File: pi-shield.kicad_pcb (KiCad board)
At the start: 4 copper layers, 65 x 56 mm, 52 parts, among them J1 Conn_02x20_Odd_Even, J10 Conn_01x04, J11 0530470210, J12 Conn_01x03, J2 Conn_01x04, J3 Conn_01x04, J4 0530470210, J5 Conn_01x05, J6 Conn_01x07, J7 0530471410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

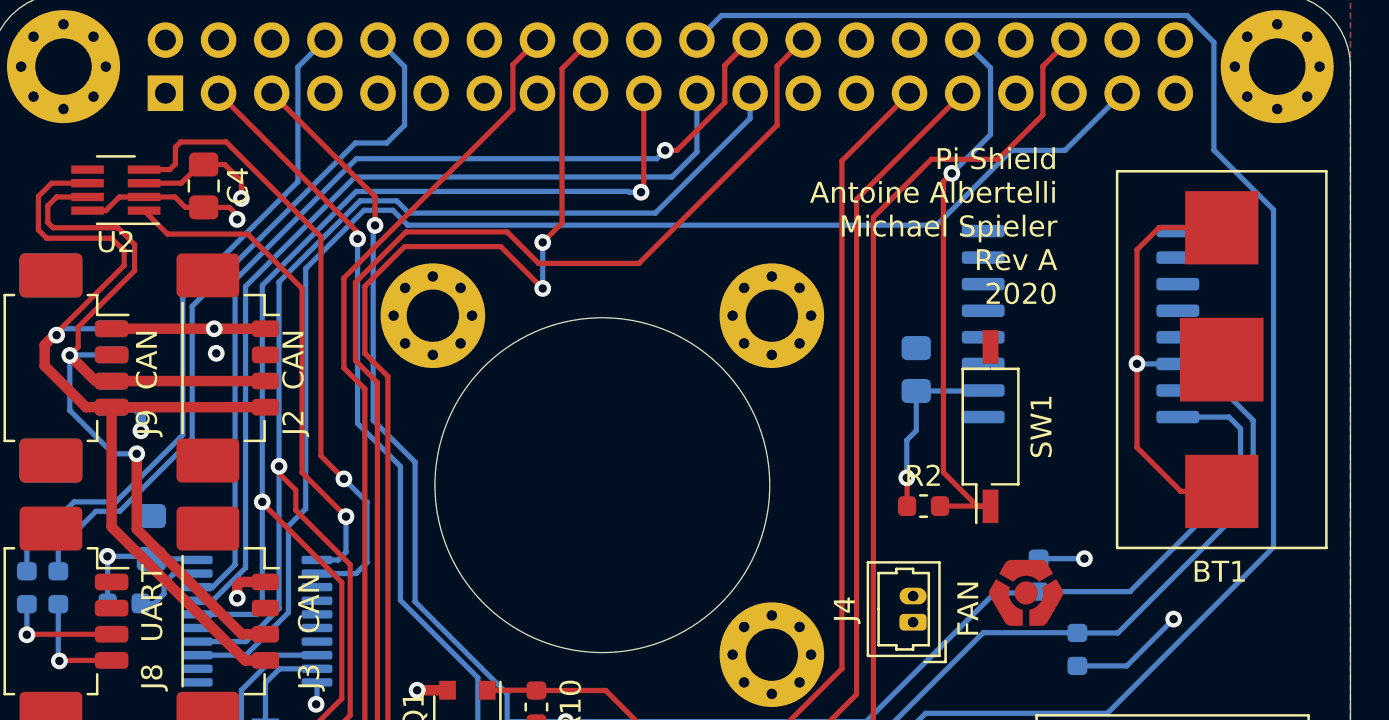
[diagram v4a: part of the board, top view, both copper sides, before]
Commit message: Add missing 3d object
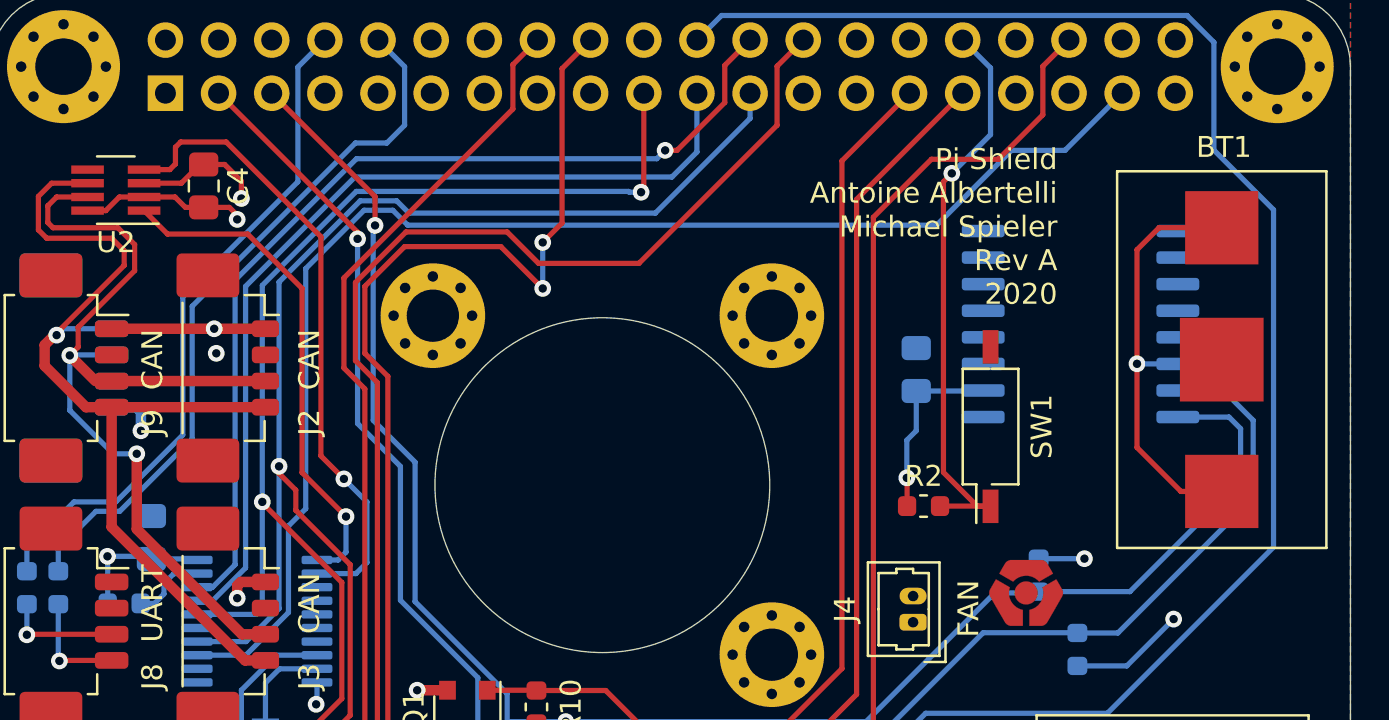
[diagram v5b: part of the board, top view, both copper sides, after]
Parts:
- turned BT1 to 270 degrees

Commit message: Corrections taking into account @nuft remarks
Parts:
- moved R10 4.53 mm to (66.8, 72.3)
- moved Q1 1.53 mm to (60.1, 72.1)
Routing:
- net /SCL: track 110.2 -> 113.2 mm
- net +5V: track 141.6 -> 143.7 mm
- net /SDA: track 115.9 -> 117.6 mm
- net VBUS: track 43.6 -> 45.0 mm
- net /BTN_START: track 100.7 -> 99.5 mm
- net /BTN_TEAM2: track 99.7 -> 98.7 mm
- net /BTN_TEAM1: track 98.7 -> 98.1 mm
- net GND: vias 9 -> 20
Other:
- outline, holes or cut-outs redrawn
- board text added: "O C"
- board text added: "Pi Shield Antoine Albertelli & Michael Spieler Rev A 2020"
- board text added: "ROBOT SELECT"
- board text removed: "Pi Shield Antoine Albertelli Michael Spieler Rev A 2020"

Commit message: Prepare for manufacturing adding all digikey#
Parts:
- removed G*** (x2): LOGO, pi-shield:CVRA-logo-small-copper
- D1: value LED -> SML-LXT0805IW-TR
- J12: footprint Connector_Molex:Molex_PicoBlade_53398-0471_1x04-1MP_P1.25mm_Vertical -> Connector_Molex:Molex_PicoBlade_53398-0371_1x03-1MP_P1.25mm_Vertical
- R3: value R_Small -> 130
- R6, R7: value 100 -> 130
- R8, R9: value 1k -> 3k24
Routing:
- net /SHDN_OK: track 68.9 -> 67.6 mm
